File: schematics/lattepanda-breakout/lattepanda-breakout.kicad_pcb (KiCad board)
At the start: 2 copper layers, 27 x 69.7 mm, 8 parts, among them J1 RJ45, J3 Conn_02x04_Odd_Even, J4 Conn_02x15_Odd_Even, J5 Conn_02x02_Odd_Even, J6 Conn_01x03_Socket, J7 Conn_01x03_Socket, J8 Conn_01x03_Socket, J9 Conn_01x03_Socket

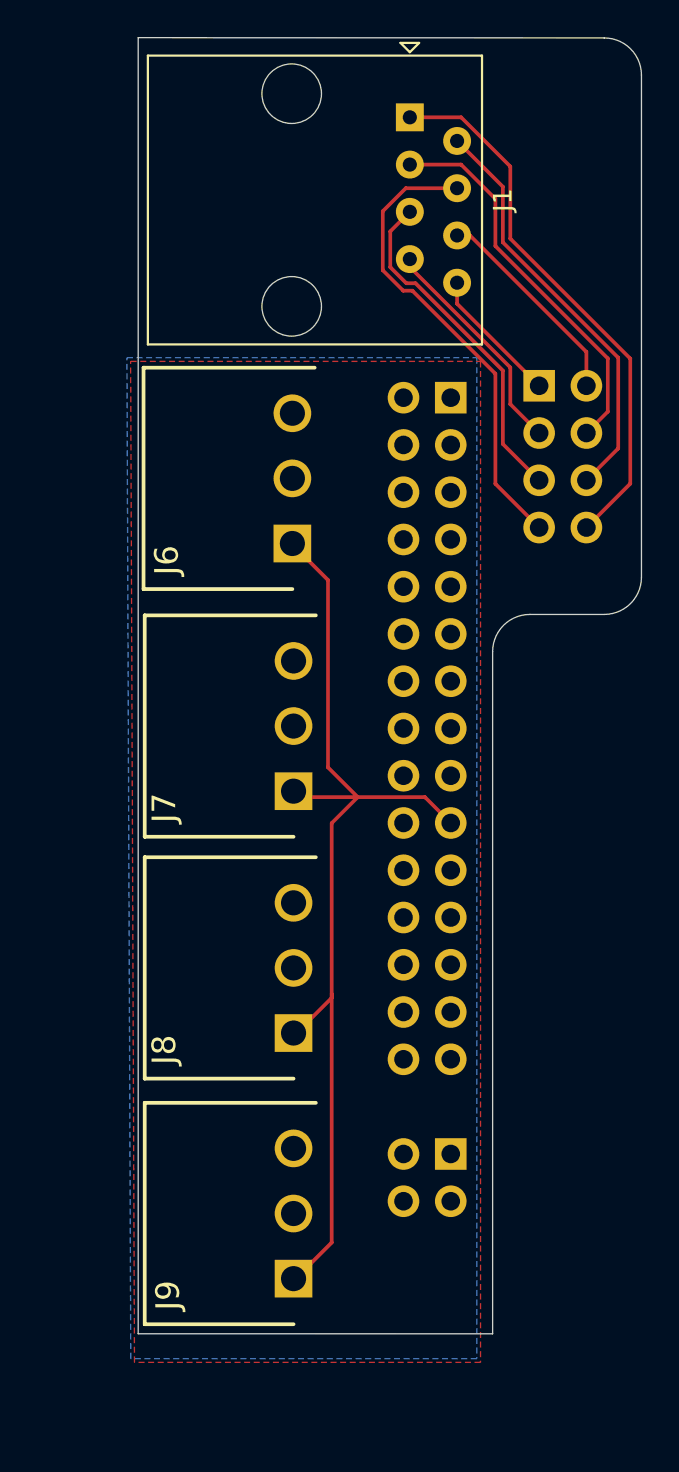
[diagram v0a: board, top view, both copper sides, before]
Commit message: open up sata
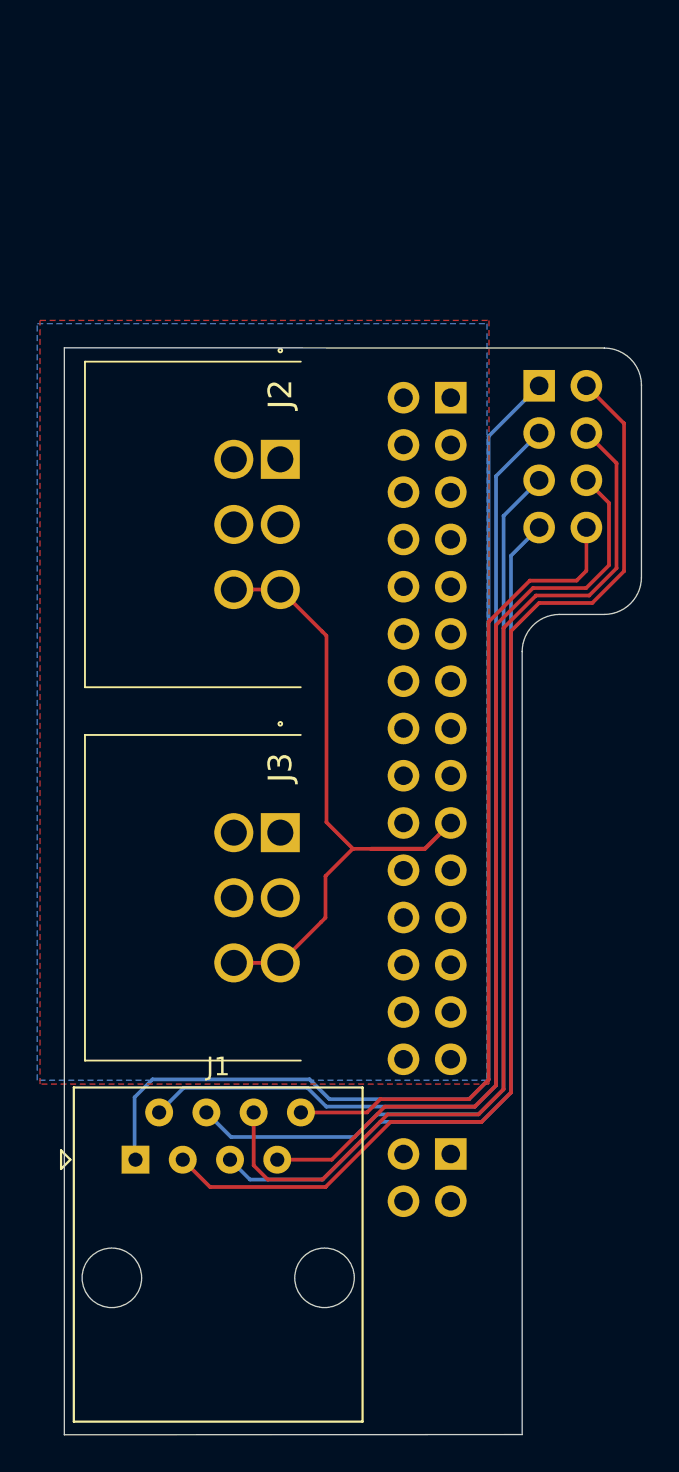
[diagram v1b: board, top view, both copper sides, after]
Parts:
- removed J8, J9: Conn_01x03_Socket, Link_Footprints:PC-1844223
- J2: renamed from J6; value Conn_01x03_Socket -> PC-1818517; footprint Link_Footprints:PC-1844223 -> Link_Footprints:PC-1818517
- J3: renamed from J7; value Conn_01x03_Socket -> PC-1818517; footprint Link_Footprints:PC-1844223 -> Link_Footprints:PC-1818517
- moved J1 57.9 mm to (86.1, 89.3), turned to 0 degrees
- moved J3 12.8 mm to (95.9, 85.0)
- moved J2 6.03 mm to (95.9, 64.9)
- renumbered J3 to J4, J4 to J5, J5 to J6
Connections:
- J1 pad 1: /BTN_RST_{-} -> /LED_PWR_{+}
- J1 pad 2: /BTN_RST_{+} -> /LED_PWR_{-}
- J1 pad 3: /LED_HDD_{-} -> /LED_HDD_{+}
- J1 pad 4: /BTN_PWR_{+} -> /BTN_PWR_{-}
- J1 pad 5: /BTN_PWR_{-} -> /BTN_PWR_{+}
- J1 pad 6: /LED_HDD_{+} -> /LED_HDD_{-}
- J1 pad 7: /LED_PWR_{-} -> /BTN_RST_{+}
- J1 pad 8: /LED_PWR_{+} -> /BTN_RST_{-}
- J2 pad 1: /SDI_COMM -> /SDI_PWR
- J2 pad 3: /SDI_PWR -> /SDI_COMM
- J3 pad 1: /SDI_COMM -> /SDI_PWR
- J3 pad 3: /SDI_PWR -> /SDI_COMM
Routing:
- net /LED_PWR_{+}: track 7.37 -> 62.1 mm
- net /LED_HDD_{+}: track 11.4 -> 63.4 mm
- net /LED_PWR_{-}: track 12.2 -> 55.6 mm
- net /LED_HDD_{-}: track 20.9 -> 58.7 mm
- net /BTN_PWR_{-}: track 18.5 -> 51.1 mm
- net /BTN_RST_{+}: track 22.5 -> 50.6 mm
- net /BTN_PWR_{+}: track 25.3 -> 48.5 mm
- net /SDI_COMM: track 54.5 -> 39.0 mm
- net /BTN_RST_{-}: track 29.5 -> 44.1 mm
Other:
- board size 27 x 69.7 mm -> 31 x 58.4 mm
